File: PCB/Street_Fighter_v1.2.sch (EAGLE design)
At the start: 42 parts, among them Q1 BSS138, Q2 BSS138, Q3 FQP30N06L, Q4 BSS138, U1 ARDUINO_YUN_SHIELDYUN, U2 MCP6231RT-E/OT

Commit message: Fixes Issue #2 and Issue #4. New XBee socket + SPI
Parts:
- removed RSSI, XB-RESET, XB-RTS: TEST-POINT3, SparkFun-Passives:TEST-POINT3
- removed TEMP: TMP36, SparkFun-Connectors:M03PTH
- removed UVD: Maxbotix 1320, SparkFun-Connectors:M04PTH
- added C3, C8, C9: 10uF, SparkFun-Capacitors:10UF-6.3V-20%(1206)
- added C4: 0.1uF, SparkFun-Capacitors:10UF-6.3V-20%(1206)
- added D1, D2, D3, D4: RED, SparkFun-LED:LED-RED1206
- added DS18B20: TMP36, SparkFun-Connectors:M03PTH
- added J1: FEMALE 2x3, SparkFun-Connectors:M03X2FEMALE
- added Q10, Q5, Q6, Q7, Q9: BSS138, SparkFun-DiscreteSemi:MOSFET-NCHANNELBSS123LT1G
- added R10, R11, R14, R15, R19, R20, R21, R24, R25, R26, R27: 4.7K, SparkFun-Passives:RESISTOR1206
- added R22, R23, R28, R29: 1K, SparkFun-Passives:RESISTOR1206
- added SONAR: MOTION, SparkFun-Connectors:M03PTH
- added U3: LM1117-3.3, SparkFun-PowerIC:V_REG_LM1117SOT223
- added XBEE-IN, XBEE-OUT: (no value), SparkFun-Retired:SOLDERJUMPER_2WAYS
- added XBEE1: XBEE-2B3, SparkFun-RF:XBEE-2B3
- LIDAR: value Lidar Lite -> LidarLite; device SparkFun-Connectors:M06SIP -> SparkFun-Connectors:M03PTH
- R1, R12, R13, R2, R3, R4: value 10K -> 4.7K
- R5: value 330R -> 2K2
- RTC: value DS1307 -> DC1307; device SparkFun-Connectors:M05PTH -> SparkFun-Connectors:M04PTH
- T-ROAD: value MLX90614-ACF? -> MLX90614-ACF
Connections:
- removed net LIDAR-CTRL: LIDAR.5
- removed net RANGE-ANALOG: U1.A1, UVD.3
- removed net RANGE-CTRL: UVD.2
- removed net SQW: RTC.3
- removed net XB-AD3: XBEE.DIO3
- removed net XB-DTR: XBEE.DTR
- removed net XB-RESET: XB-RESET.1, XBEE.RESET
- removed net XB-RTS: XB-RTS.1, XBEE.RTS
- new net MISO: J1.1, Q5.D, R14.1
- new net MOSI: J1.4, Q6.D, R19.1
- new net N$1: D1.A, R22.2
- new net N$3: D2.A, R23.2
- new net N$5: D3.A, R28.2
- new net N$6: D4.A, R29.2
- new net RST: J1.5
- new net RX-XB2: Q10.D, R27.1, U1.D11*
- new net SCK: J1.3, Q7.D, R21.1
- new net SONAR-PULSEIN: SONAR.2, U1.A0
- new net TX-XB2: Q9.D, R25.1, U1.D12*
- new net XB-ASSO: R22.1, XBEE.DIO5
- new net XB-ATTN: XBEE-OUT.1, XBEE.DIO1
- new net XB-DIN: XBEE-IN.3, XBEE.DIN
- new net XB-DOUT: XBEE-OUT.3, XBEE.DOUT
- new net XB-MISO: Q5.S, R11.1, XBEE.DIO12
- new net XB-MOSI: Q6.S, R15.1, XBEE.DIO4
- new net XB-SCK: Q7.S, R20.1, XBEE.DIO2
- new net XB-SS: XBEE-IN.1, XBEE.DIO3
- new net XB2-ASSO: R28.1, XBEE1.DIO5
- new net XB2-DIN: Q9.S, R24.1, XBEE1.DIN
- new net XB2-DOUT: Q10.S, R26.1, XBEE1.DOUT
- new net XB2-RSSI: R29.1, XBEE1.RSSI
- net +3V3: now also C3.2, C4.2, C9.2, Q10.G, Q5.G, Q6.G, Q7.G, Q9.G, R11.2, R15.2, R20.2, R24.2, R26.2, U3.OUT, U3.OUT@1, XBEE1.VDD; no longer U1.3V3
- net +5V: now also C8.2, DS18B20.3, J1.2, LIDAR.3, R10.2, R14.2, R19.2, R21.2, R25.2, R27.2, RTC.4, SONAR.3, U3.IN; no longer LIDAR.6, RTC.5, TEMP.3, UVD.4
- net GND: now also C3.1, C4.1, C8.1, C9.1, D1.C, D2.C, D3.C, D4.C, DS18B20.1, J1.6, RTC.1, SONAR.1, U3.ADJ, XBEE1.GND; no longer RTC.4, TEMP.1, UVD.1
- net LIDAR-PWM: now also LIDAR.2; no longer LIDAR.4
- net SCL: no longer LIGHT.2, RTC.2
- net SCL@1: now also LIGHT.2, RTC.2
- net SDA: no longer LIGHT.3, RTC.1
- net SDA@1: now also LIGHT.3, RTC.3
- net TEMP: now also DS18B20.2, R10.1; no longer TEMP.2
- net XB-RSSI: now also R23.1; no longer RSSI.1
- net XB-RX3V: now also XBEE-OUT.2; no longer XBEE.DOUT
- net XB-SLEEP3V: now also XBEE1.DIO9
- net XB-TX3V: now also XBEE-IN.2; no longer XBEE.DIN
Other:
- note added: "ICSP Header"
- note added: "Levels - SPI"
- note added: "Levels - XBee 1"
- note added: "Levels - XBee 2"
- note added: "XBee Power"
- note added: "XBee Socket 1"
- note added: "XBee Socket 2"
- note removed: "Pin 3 - Analog out"
- note removed: "Pin 4 - Control (active high)"
- note removed: "XBee Transceiver"
- moved on the sheet: C1, C2, C5, C6, C7, CURRENT, HUMD, JP2, JP3, JP4, LIGHT, PIR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

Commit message: Added spare header to board
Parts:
- added SPARE: A1, SparkFun-Connectors:M03PTH
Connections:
- new net SPARE: SPARE.2, U1.A1
- net +5V: now also SPARE.3
- net GND: now also SPARE.1
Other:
- note added: "Spare"
- note removed: "Base Components"
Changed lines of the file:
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@@
 <part name="RTC" library="SparkFun-Connectors" deviceset="M04" device="PTH" value="DC1307"/>
 <part name="LIDAR" library="SparkFun-Connectors" deviceset="M03" device="PTH" value="LidarLite"/>
+<part name="P+28" library="supply1" deviceset="+5V" device=""/>
+<part name="GND30" library="supply1" deviceset="GND" device=""/>
+<part name="SPARE" library="SparkFun-Connectors" deviceset="M03" device="PTH" value="A1"/>
 </parts>
 <sheets>
@@
 <text x="340.36" y="204.47" size="2.54" layer="97" ratio="15">Current Monitor</text>
 <text x="109.22" y="151.13" size="2.54" layer="97" ratio="15">XBee Socket 1</text>
-<text x="33.02" y="619.76" size="6.4516" layer="91" ratio="15">Base
-Components</text>
 <text x="39.116" y="44.196" size="2.54" layer="115" ratio="15">Sonar</text>
 <text x="170.688" y="43.688" size="2.54" layer="114" ratio="15">Illuminance</text>
@@
 <wire x1="378.46" y1="195.58" x2="337.82" y2="195.58" width="0.6096" layer="97"/>
 <text x="338.582" y="173.482" size="2.032" layer="97" ratio="15">ICSP Header</text>
+<text x="340.868" y="43.688" size="2.54" layer="114" ratio="15">Spare</text>
+<wire x1="340.36" y1="43.18" x2="340.36" y2="73.66" width="0.4064" layer="114"/>
+<wire x1="340.36" y1="73.66" x2="368.3" y2="73.66" width="0.4064" layer="114"/>
+<wire x1="368.3" y1="73.66" x2="368.3" y2="43.18" width="0.4064" layer="114"/>
+<wire x1="368.3" y1="43.18" x2="340.36" y2="43.18" width="0.4064" layer="114"/>
 </plain>
 <instances>
@@
 <attribute name="NAME" x="106.68" y="66.802" size="1.778" layer="95"/>
 </instance>
+<instance part="P+28" gate="1" x="358.14" y="71.12"/>
+<instance part="GND30" gate="1" x="355.6" y="50.8"/>
+<instance part="SPARE" gate="G$1" x="345.44" y="60.96"/>
 </instances>
 <busses>
@@
 <wire x1="368.3" y1="187.96" x2="368.3" y2="190.5" width="0.2032" layer="91"/>
 <wire x1="365.76" y1="187.96" x2="368.3" y2="187.96" width="0.2032" layer="91"/>
+</segment>
+<segment>
+<pinref part="SPARE" gate="G$1" pin="3"/>
+<pinref part="P+28" gate="1" pin="+5V"/>
+<wire x1="353.06" y1="63.5" x2="358.14" y2="63.5" width="0.2032" layer="91"/>
+<wire x1="358.14" y1="63.5" x2="358.14" y2="68.58" width="0.2032" layer="91"/>
 </segment>
 </net>
@@
 <wire x1="218.44" y1="124.46" x2="218.44" y2="119.38" width="0.2032" layer="91"/>
 </segment>
+<segment>
+<pinref part="SPARE" gate="G$1" pin="1"/>
+<pinref part="GND30" gate="1" pin="GND"/>
+<wire x1="353.06" y1="58.42" x2="355.6" y2="58.42" width="0.2032" layer="91"/>
+<wire x1="355.6" y1="58.42" x2="355.6" y2="53.34" width="0.2032" layer="91"/>
+</segment>
 </net>
 <net name="TEMP" class="0">
@@
 </segment>
 </net>
+<net name="SPARE" class="0">
+<segment>
+<label x="355.6" y="60.96" size="1.27" layer="95" xref="yes"/>
+<wire x1="355.6" y1="60.96" x2="353.06" y2="60.96" width="0.2032" layer="91"/>
+<pinref part="SPARE" gate="G$1" pin="2"/>
+</segment>
+<segment>
+<pinref part="U1" gate="G$1" pin="A1"/>
+<wire x1="33.02" y1="195.58" x2="27.94" y2="195.58" width="0.2032" layer="91"/>
+<label x="27.94" y="195.58" size="1.27" layer="95" rot="R180" xref="yes"/>
+</segment>
+</net>
 </nets>
 </sheet>
@@
 </schematic>
 </drawing>
-<compatibility>
-<note version="6.3" minversion="6.2.2" severity="warning">
-Since Version 6.2.2 text objects can contain more than one line,
-which will not be processed correctly with this version.
-</note>
-</compatibility>
 </eagle>

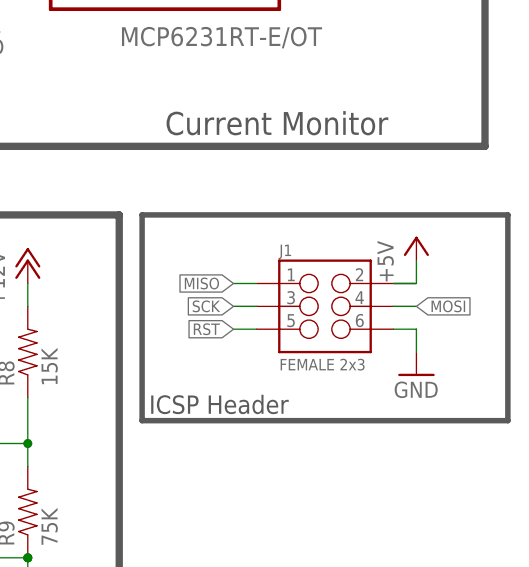
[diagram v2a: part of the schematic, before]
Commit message: StreetFighter v1.3 board - Fixed bad pin assignments for SoftSerial
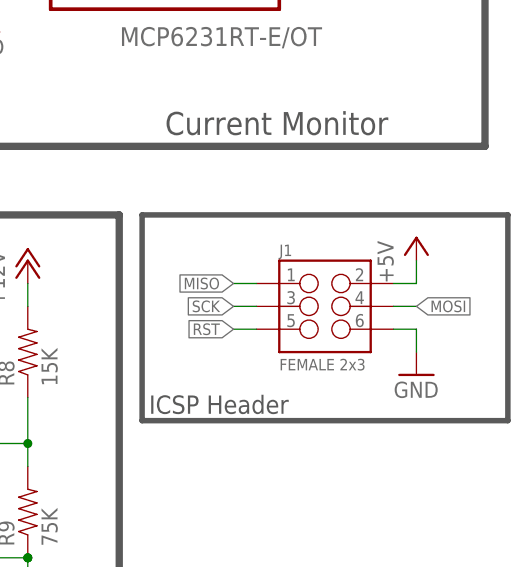
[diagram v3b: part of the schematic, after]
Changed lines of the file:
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@@
 <segment>
 <pinref part="J1" gate="G$1" pin="2"/>
-<wire x1="365.76" y1="187.96" x2="368.3" y2="187.96" width="0.2032" layer="91"/>
 <pinref part="P+31" gate="1" pin="+5V"/>
 <wire x1="368.3" y1="187.96" x2="368.3" y2="190.5" width="0.2032" layer="91"/>
